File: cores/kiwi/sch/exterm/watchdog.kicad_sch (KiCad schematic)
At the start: 18 parts, among them J8 TL7705A, SW1 SW_Push

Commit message: issue#46
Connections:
- net ~{WATCHDOG} renamed WATCHDOG
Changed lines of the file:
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@@
     (effects (font (size 1.27 1.27)) (justify left bottom))
   )
-  (hierarchical_label "~{WATCHDOG}" (shape input) (at 87.63 100.33 180)
+  (hierarchical_label "WATCHDOG" (shape input) (at 87.63 100.33 180)
     (effects (font (size 1.27 1.27)) (justify right))
   )

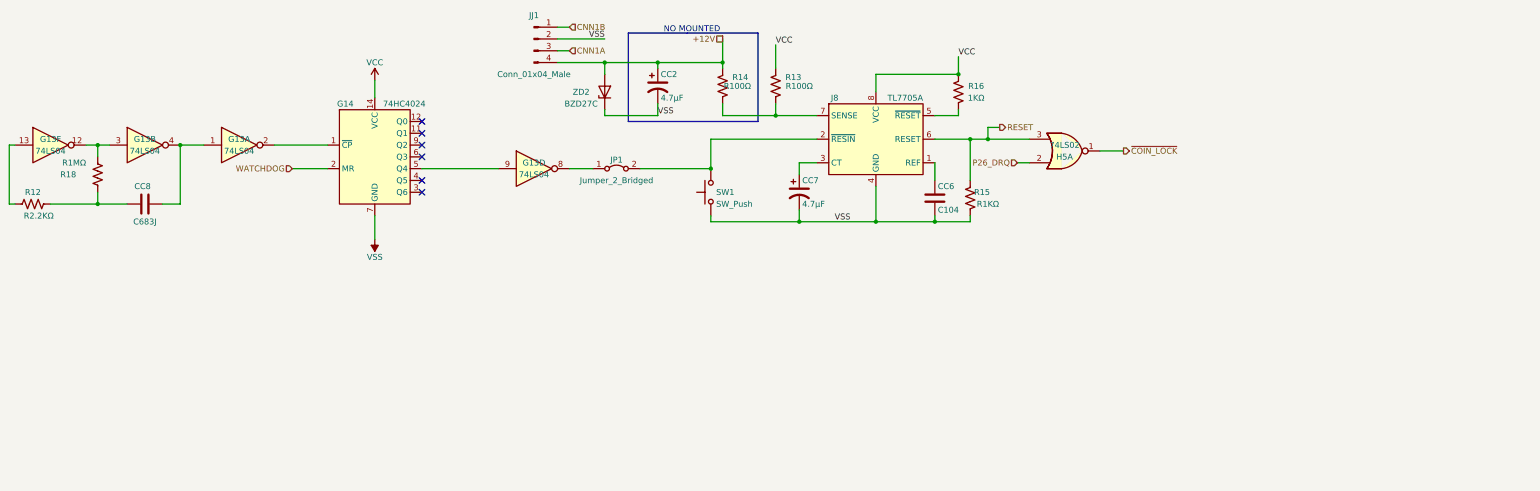
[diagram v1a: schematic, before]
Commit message: sheet_size_update
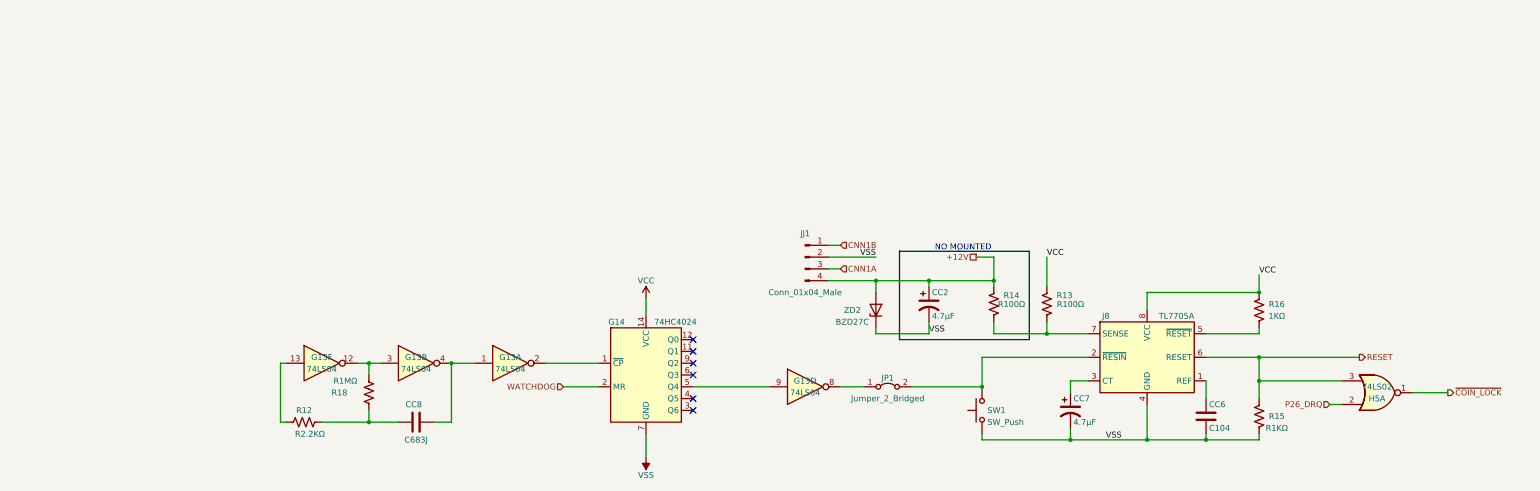
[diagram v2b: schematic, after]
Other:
- moved on the sheet: CC2, CC6, CC7, CC8, G13A, G13B, G13D, G13F, G14, H5A, J8, JJ1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
